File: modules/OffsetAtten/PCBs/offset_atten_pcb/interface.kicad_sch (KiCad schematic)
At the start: 14 parts, among them J1 THONKICONN, J2 THONKICONN, J3 THONKICONN, J4 THONKICONN

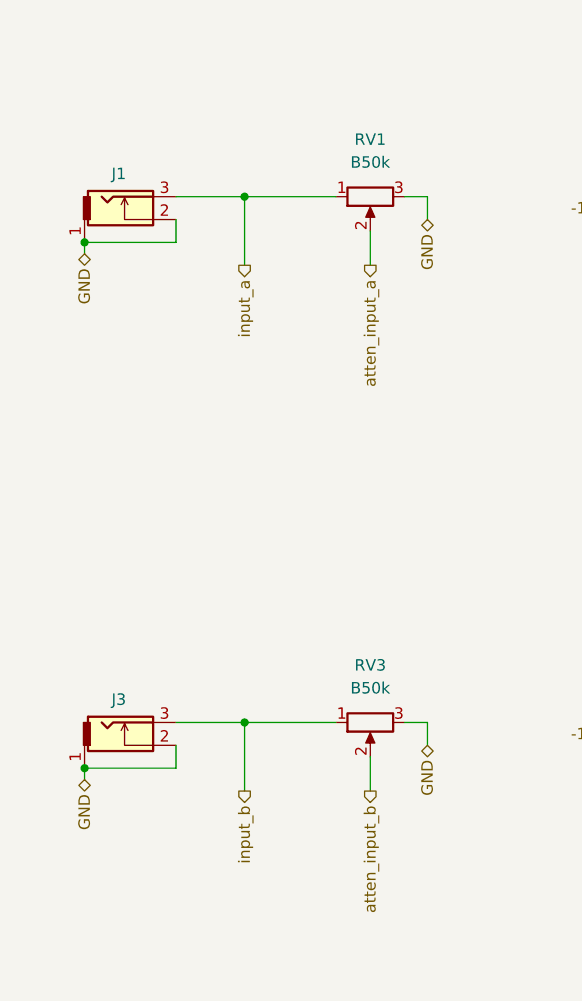
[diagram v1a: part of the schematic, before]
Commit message: Add buffer to O/A; (see #67) closes #62
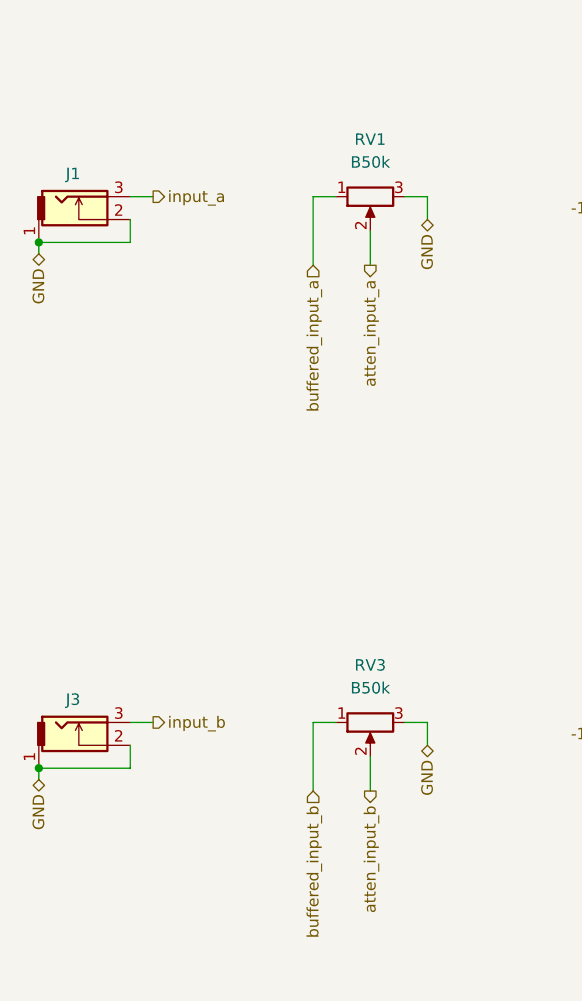
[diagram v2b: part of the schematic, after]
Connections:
- net input_a: no longer RV1.1
- net input_b: no longer RV3.1
- new net buffered_input_a: RV1.1
- new net buffered_input_b: RV3.1
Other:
- moved on the sheet: J1, J3
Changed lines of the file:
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@@
 (kicad_sch
-	(version 20231120)
+	(version 20250114)
 	(generator "eeschema")
-	(generator_version "8.0")
+	(generator_version "9.0")
 	(paper "A4")
 	(title_block
 		(title "OffsetAtten")
-		(date "2024-05-01")
-		(rev "v2.0")
+		(date "2025-04-23")
+		(rev "v2.1")
 		(company "Free Modular")
 	)
 	(junction
-		(at 76.2 124.46)
+		(at 53.34 129.54)
 		(diameter 0)
 		(color 0 0 0 0)
 	)
 	(junction
-		(at 76.2 66.04)
+		(at 53.34 71.12)
 		(diameter 0)
 		(color 0 0 0 0)
 	)
-	(junction
-		(at 58.42 129.54)
-		(diameter 0)
-		(color 0 0 0 0)
-	)
-	(junction
-		(at 58.42 71.12)
-		(diameter 0)
-		(color 0 0 0 0)
-	)
 	(no_connect
 		(at 187.96 132.08)
@@
 	(wire
 		(pts
-			(xy 68.58 127) (xy 68.58 129.54)
+			(xy 63.5 127) (xy 63.5 129.54)
 		)
 		(stroke
@@
 	(wire
 		(pts
-			(xy 68.58 129.54) (xy 58.42 129.54)
+			(xy 63.5 129.54) (xy 53.34 129.54)
 		)
 		(stroke
@@
 	(wire
 		(pts
-			(xy 76.2 66.04) (xy 76.2 73.66)
-		)
-		(stroke
-			(width 0)
-			(type default)
-		)
-	)
-	(wire
-		(pts
 			(xy 140.97 63.5) (xy 144.78 63.5)
 		)
@@
 	(wire
 		(pts
-			(xy 68.58 68.58) (xy 68.58 71.12)
+			(xy 63.5 68.58) (xy 63.5 71.12)
 		)
 		(stroke
@@
 	(wire
 		(pts
+			(xy 83.82 124.46) (xy 86.36 124.46)
+		)
+		(stroke
+			(width 0)
+			(type default)
+		)
+	)
+	(wire
+		(pts
 			(xy 121.92 121.92) (xy 119.38 121.92)
 		)
@@
 	(wire
 		(pts
-			(xy 68.58 71.12) (xy 58.42 71.12)
+			(xy 63.5 71.12) (xy 53.34 71.12)
 		)
 		(stroke
@@
 	(wire
 		(pts
-			(xy 76.2 124.46) (xy 86.36 124.46)
-		)
-		(stroke
-			(width 0)
-			(type default)
-		)
-	)
-	(wire
-		(pts
 			(xy 118.11 125.73) (xy 119.38 125.73)
 		)
@@
 	(wire
 		(pts
-			(xy 76.2 66.04) (xy 86.36 66.04)
-		)
-		(stroke
-			(width 0)
-			(type default)
-		)
-	)
-	(wire
-		(pts
-			(xy 58.42 130.81) (xy 58.42 129.54)
-		)
-		(stroke
-			(width 0)
-			(type default)
-		)
-	)
-	(wire
-		(pts
-			(xy 68.58 66.04) (xy 76.2 66.04)
-		)
-		(stroke
-			(width 0)
-			(type default)
-		)
-	)
-	(wire
-		(pts
-			(xy 76.2 132.08) (xy 76.2 124.46)
+			(xy 53.34 130.81) (xy 53.34 129.54)
+		)
+		(stroke
+			(width 0)
+			(type default)
+		)
+	)
+	(wire
+		(pts
+			(xy 63.5 66.04) (xy 66.04 66.04)
 		)
 		(stroke
@@
 	(wire
 		(pts
+			(xy 83.82 66.04) (xy 86.36 66.04)
+		)
+		(stroke
+			(width 0)
+			(type default)
+		)
+	)
+	(wire
+		(pts
 			(xy 90.17 69.85) (xy 90.17 73.66)
 		)
@@
 	(wire
 		(pts
-			(xy 58.42 72.39) (xy 58.42 71.12)
+			(xy 53.34 72.39) (xy 53.34 71.12)
 		)
 		(stroke
@@
 	(wire
 		(pts
-			(xy 68.58 124.46) (xy 76.2 124.46)
+			(xy 83.82 66.04) (xy 83.82 73.66)
+		)
+		(stroke
+			(width 0)
+			(type default)
+		)
+	)
+	(wire
+		(pts
+			(xy 63.5 124.46) (xy 66.04 124.46)
 		)
 		(stroke
@@
 	(wire
 		(pts
+			(xy 83.82 124.46) (xy 83.82 132.08)
+		)
+		(stroke
+			(width 0)
+			(type default)
+		)
+	)
+	(wire
+		(pts
 			(xy 140.97 121.92) (xy 144.78 121.92)
 		)
@@
 		(shape bidirectional)
 		(at 118.11 125.73 180)
-		(fields_autoplaced yes)
 		(effects
 			(font
@@
 		(shape input)
 		(at 185.42 129.54 180)
-		(fields_autoplaced yes)
 		(effects
 			(font
@@
 		(shape bidirectional)
 		(at 96.52 68.58 270)
-		(fields_autoplaced yes)
 		(effects
 			(font
@@
 	(hierarchical_label "input_a"
 		(shape output)
-		(at 76.2 73.66 270)
-		(fields_autoplaced yes)
-		(effects
-			(font
-				(size 1.27 1.27)
-			)
-			(justify right)
+		(at 66.04 66.04 0)
+		(effects
+			(font
+				(size 1.27 1.27)
+			)
+			(justify left)
 		)
 	)
 	(hierarchical_label "GND"
 		(shape bidirectional)
-		(at 58.42 130.81 270)
-		(fields_autoplaced yes)
+		(at 53.34 130.81 270)
 		(effects
 			(font
@@
 		(shape bidirectional)
 		(at 182.88 50.8 180)
-		(fields_autoplaced yes)
 		(effects
 			(font
@@
 		(shape output)
 		(at 90.17 132.08 270)
-		(fields_autoplaced yes)
+		(effects
+			(font
+				(size 1.27 1.27)
+			)
+			(justify right)
+		)
+	)
+	(hierarchical_label "buffered_input_a"
+		(shape input)
+		(at 83.82 73.66 270)
 		(effects
 			(font
@@
 		(shape output)
 		(at 137.16 69.85 270)
-		(fields_autoplaced yes)
 		(effects
 			(font
@@
 	(hierarchical_label "GND"
 		(shape bidirectional)
-		(at 58.42 72.39 270)
-		(fields_autoplaced yes)
+		(at 53.34 72.39 270)
 		(effects
 			(font
@@
 		(shape bidirectional)
 		(at 96.52 127 270)
-		(fields_autoplaced yes)
 		(effects
 			(font
@@
 		(shape bidirectional)
 		(at 198.12 76.2 270)
-		(fields_autoplaced yes)
 		(effects
 			(font
@@
 		(shape bidirectional)
 		(at 118.11 67.31 180)
-		(fields_autoplaced yes)
 		(effects
 			(font
@@
 	(hierarchical_label "input_b"
 		(shape output)
-		(at 76.2 132.08 270)
-		(fields_autoplaced yes)
-		(effects
-			(font
-				(size 1.27 1.27)
-			)
-			(justify right)
+		(at 66.04 124.46 0)
+		(effects
+			(font
+				(size 1.27 1.27)
+			)
+			(justify left)
 		)
 	)
@@
 		(shape input)
 		(at 185.42 71.12 180)
-		(fields_autoplaced yes)
+		(effects
+			(font
+				(size 1.27 1.27)
+			)
+			(justify right)
+		)
+	)
+	(hierarchical_label "buffered_input_b"
+		(shape input)
+		(at 83.82 132.08 270)
 		(effects
 			(font
@@
 		(shape bidirectional)
 		(at 198.12 134.62 270)
-		(fields_autoplaced yes)
 		(effects
 			(font
@@
 		(shape bidirectional)
 		(at 198.12 50.8 0)
-		(fields_autoplaced yes)
 		(effects
 			(font
@@
 		(shape bidirectional)
 		(at 180.34 109.22 180)
-		(fields_autoplaced yes)
 		(effects
 			(font
@@
 		(shape bidirectional)
 		(at 195.58 109.22 0)
-		(fields_autoplaced yes)
 		(effects
 			(font
@@
 		(shape output)
 		(at 137.16 128.27 270)
-		(fields_autoplaced yes)
 		(effects
 			(font
@@
 		(shape bidirectional)
 		(at 157.48 118.11 0)
-		(fields_autoplaced yes)
 		(effects
 			(font
@@
 		(shape output)
 		(at 90.17 73.66 270)
-		(fields_autoplaced yes)
 		(effects
 			(font
@@
 		(shape bidirectional)
 		(at 157.48 59.69 0)
-		(fields_autoplaced yes)
 		(effects
 			(font
@@
 	(symbol
 		(lib_id "FreeModular:THONKICONN")
-		(at 63.5 68.58 0)
+		(at 58.42 68.58 0)
 		(unit 1)
 		(exclude_from_sim no)
@@
 		(fields_autoplaced yes)
 		(property "Reference" "J1"
-			(at 62.23 63.5 0)
+			(at 57.15 63.5 0)
 			(effects
 				(font
@@
 		)
 		(property "Value" "THONKICONN"
-			(at 64.77 71.12 0)
+			(at 59.69 71.12 0)
 			(effects
 				(font
@@
 		)
 		(property "Footprint" "FreeModular:THONKICONN_perf"
-			(at 69.85 66.04 0)
+			(at 64.77 66.04 0)
 			(effects
 				(font
@@
 		)
 		(property "Datasheet" "~"
-			(at 69.85 66.04 0)
+			(at 64.77 66.04 0)
 			(effects
 				(font
@@
 		)
 		(property "Description" "2-pin audio jack receptable (mono/TS connector) with switching contact"
-			(at 63.5 68.58 0)
+			(at 58.42 68.58 0)
 			(effects
 				(font
@@
 	(symbol
 		(lib_id "FreeModular:THONKICONN")
-		(at 63.5 127 0)
+		(at 58.42 127 0)
 		(unit 1)
 		(exclude_from_sim no)
@@
 		(fields_autoplaced yes)
 		(property "Reference" "J3"
-			(at 62.23 121.92 0)
+			(at 57.15 121.92 0)
 			(effects
 				(font
@@
 		)
 		(property "Value" "THONKICONN"
-			(at 64.77 129.54 0)
+			(at 59.69 129.54 0)
 			(effects
 				(font
@@
 		)
 		(property "Footprint" "FreeModular:THONKICONN_perf"
-			(at 69.85 124.46 0)
+			(at 64.77 124.46 0)
 			(effects
 				(font
@@
 		)
 		(property "Datasheet" "~"
-			(at 69.85 124.46 0)
+			(at 64.77 124.46 0)
 			(effects
 				(font
@@
 		)
 		(property "Description" "2-pin audio jack receptable (mono/TS connector) with switching contact"
-			(at 63.5 127 0)
-			(effects
-				(font
+			(at 58.42 127 0)
+			(effects
+				(font
